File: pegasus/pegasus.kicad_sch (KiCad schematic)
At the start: 18 parts, among them IC1 L7805ACV, IC2 RFD900, IC3 L70B-M39, J2 Screw_Terminal_01x02, U1 Teensy4.0, U2 CON-SMA-EDGE-S, U3 CON-SMA-EDGE-S, U4 XTSD04GCLGEGA

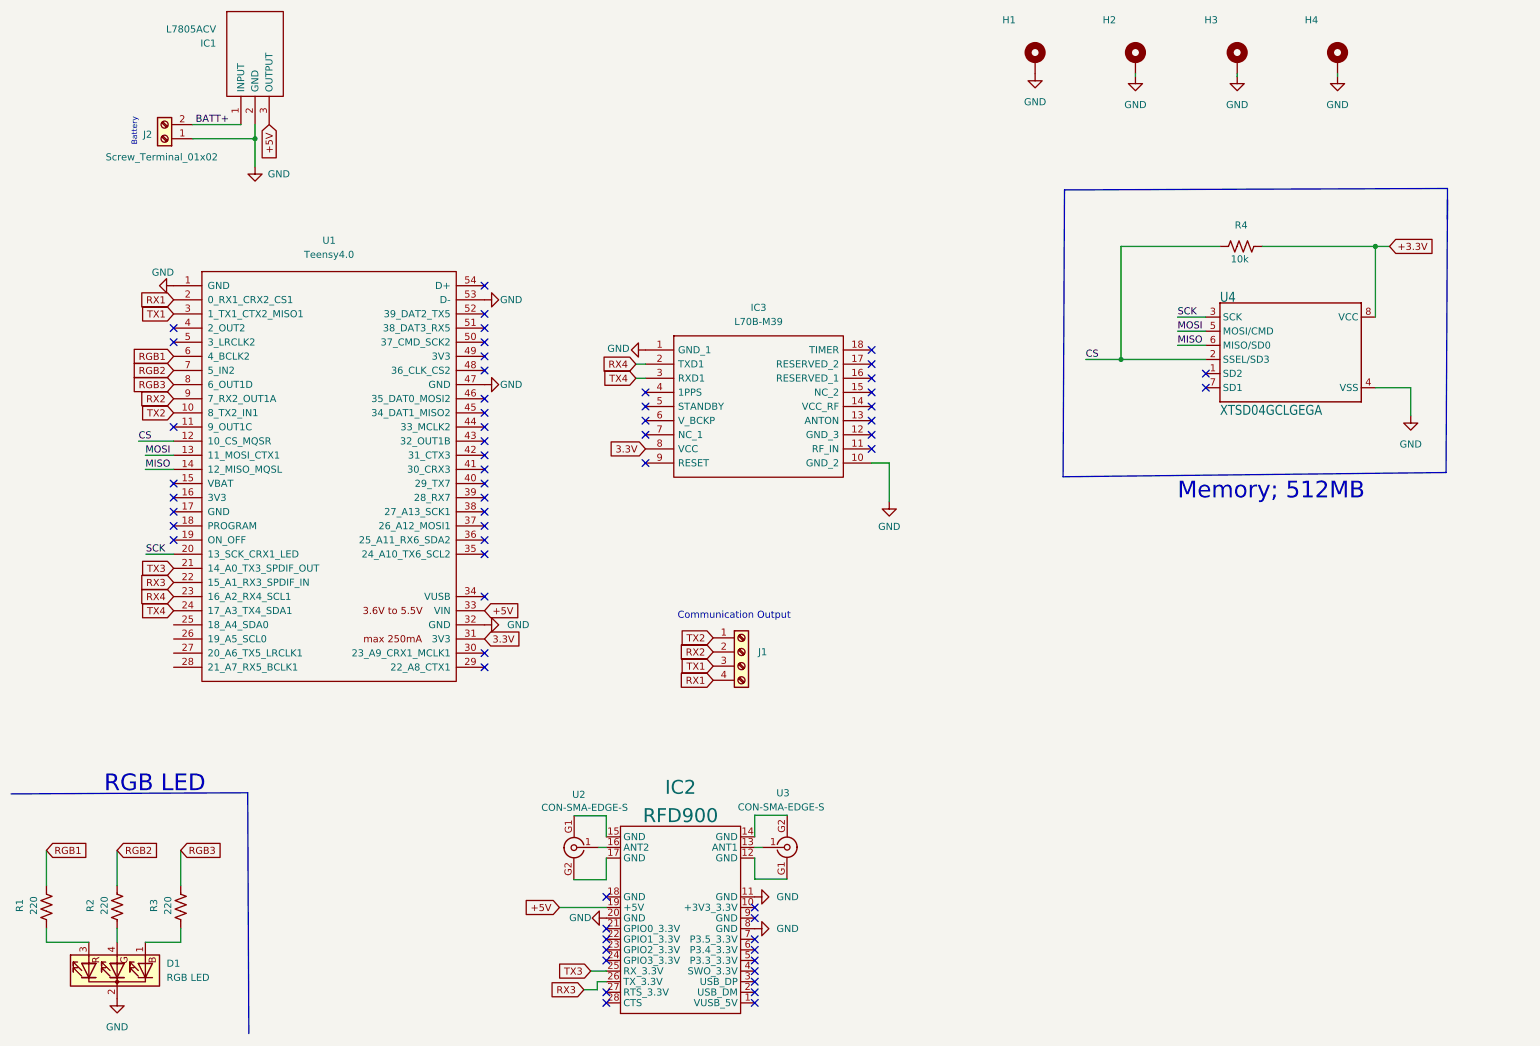
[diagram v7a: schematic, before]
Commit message: add borders and titles to components in schematic
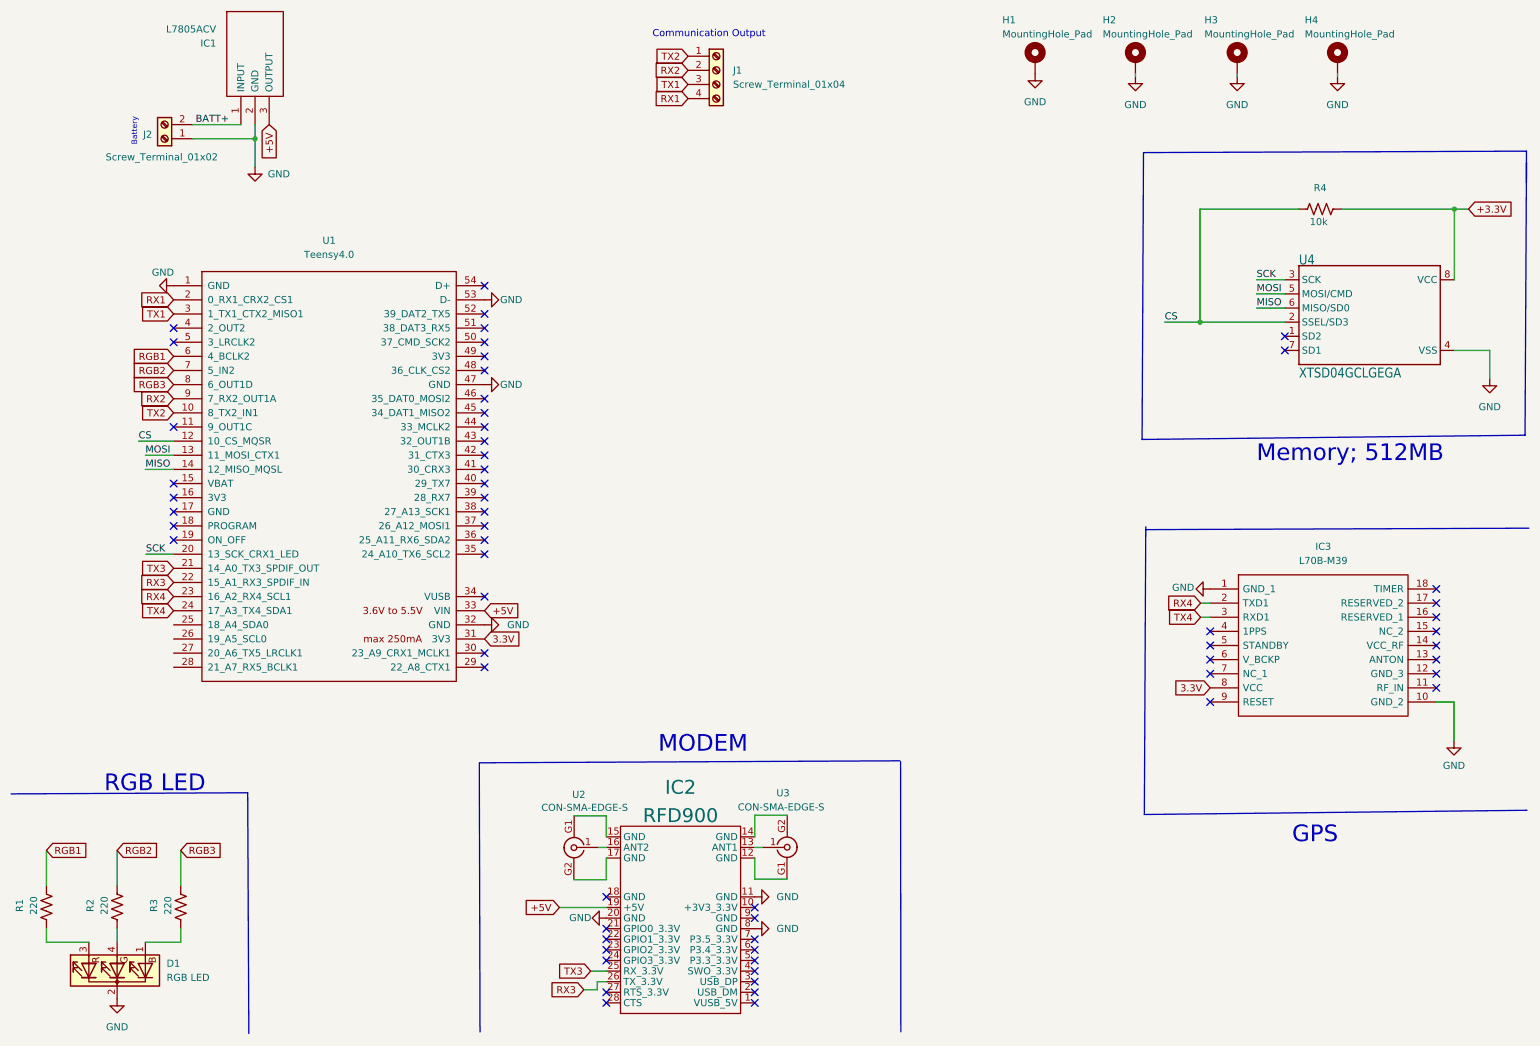
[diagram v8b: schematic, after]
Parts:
- H1, H2, H3, H4: value (none) -> MountingHole_Pad; footprint (none) -> MountingHole:MountingHole_3.2mm_M3_Pad
- J1: value (none) -> Screw_Terminal_01x04; footprint (none) -> RS-Components:SHDR4W100P0X500_1X4_2000X800X1000P
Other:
- note added: "GPS"
- note added: "MODEM"
- moved on the sheet: IC3, J1, R4, U4
